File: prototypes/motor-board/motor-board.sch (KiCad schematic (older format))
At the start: 15 parts, among them J1 Conn_01x02, J2 Conn_01x02, J3 Conn_01x01, M1 Motor_DC, U1 TLV9051, U2 TB67H450FNG

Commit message: Correct sense resistor value
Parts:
- R3: value 1R2 -> 400m
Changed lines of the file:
@@
 P 4200 4125
 F 0 "R3" H 4270 4171 50  0000 L CNN
-F 1 "1R2" H 4270 4080 50  0000 L CNN
+F 1 "400m" H 4270 4080 50  0000 L CNN
 F 2 "" V 4130 4125 50  0001 C CNN
 F 3 "~" H 4200 4125 50  0001 C CNN

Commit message: Add some footprints to library symbols
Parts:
- R1, R2, R3, R4, R5, R6: footprint (none) -> mini-mapper:R_0805
- U2: footprint (none) -> mini-mapper:SOIC127P600X175-9N
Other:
- note added: "Current limiting reference voltage"
- note added: "Current sense resistor"
- note added: "Current: 0 ≤ I ≤ 250 mA\nKeep Vsense ≤ 100 mV\n\nRsense = 0.4 Ω ⇒\n 0 ≤ Vsense ≤ 0.1 V\n\n(Pmax = 25 mW)\n"
- note added: "Iout(max) = 0.1 Vref / Rsense\n\nWant Iout(max) = 250 mA\nwith VM = 4.5 V\n\nSetting Rsense = 0.4 Ω\n\nVref = 10 x 0.25 x 0.4 = 1 V\n"
- note removed: "Current sense resistor\nCurrent: 0 ≤ I ≤ 250 mA\nKeep Vsense ≤ 100 mV\nMax Rsense = 0.4 Ω ⇒\n 0 ≤ V ≤ 0.1 V\n(Pmax = 25 mW)\n"
- note removed: "Set current limiting\nreference voltage\n\nIout(max) = 0.1 Vref / Rsense\n\nWant Iout(max) = 250 mA\nwith VM = 4.5 V\n\nWith Rsense = 0.4 Ω\n\nVref = 10 x 0.25 x 0.4 = 1 V\n"
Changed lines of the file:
@@
 F 0 "U2" H 4200 3825 50  0000 C CNN
 F 1 "TB67H450FNG" H 4000 3500 50  0000 C CNN
-F 2 "" H 4100 3300 50  0001 C CNN
-F 3 "" H 4100 3300 50  0001 C CNN
+F 2 "mini-mapper:SOIC127P600X175-9N" H 4100 3300 50  0001 C CNN
+F 3 "https://www.mouser.com/pdfDocs/TB67H450FNG_datasheet_en_20190401.pdf" H 4100 3300 50  0001 C CNN
 	1    4000 3350
 	1    0    0    -1
@@
 F 0 "R3" H 4270 4171 50  0000 L CNN
 F 1 "400m" H 4270 4080 50  0000 L CNN
-F 2 "" V 4130 4125 50  0001 C CNN
+F 2 "mini-mapper:R_0805" V 4130 4125 50  0001 C CNN
 F 3 "~" H 4200 4125 50  0001 C CNN
 	1    4200 4125
@@
 Wire Wire Line
 	4000 4350 4000 4400
-Text Notes 3650 5175 0    50   ~ 0
-Current sense resistor\nCurrent: 0 ≤ I ≤ 250 mA\nKeep Vsense ≤ 100 mV\nMax Rsense = 0.4 Ω ⇒\n   0 ≤ V ≤ 0.1 V\n(Pmax = 25 mW)\n
+Text Notes 3625 4800 0    50   Italic 10
+Current sense resistor
 $Comp
 L mini-mapper:VM #PWR09
@@
 F 0 "R1" H 2820 4021 50  0000 L CNN
 F 1 "7K" H 2820 3930 50  0000 L CNN
-F 2 "" V 2680 3975 50  0001 C CNN
+F 2 "mini-mapper:R_0805" V 2680 3975 50  0001 C CNN
 F 3 "~" H 2750 3975 50  0001 C CNN
 	1    2750 3975
@@
 F 0 "R2" H 2820 4421 50  0000 L CNN
 F 1 "2K" H 2820 4330 50  0000 L CNN
-F 2 "" V 2680 4375 50  0001 C CNN
+F 2 "mini-mapper:R_0805" V 2680 4375 50  0001 C CNN
 F 3 "~" H 2750 4375 50  0001 C CNN
 	1    2750 4375
@@
 Wire Wire Line
 	3150 4650 3150 4625
-Text Notes 1375 4900 0    50   ~ 0
-Set current limiting\nreference voltage\n\nIout(max) = 0.1 Vref / Rsense\n\nWant Iout(max) = 250 mA\nwith VM = 4.5 V\n\nWith Rsense = 0.4 Ω\n\nVref = 10 x 0.25 x 0.4 = 1 V\n
+Text Notes 1125 3850 0    50   Italic 10
+Current limiting reference voltage
 Wire Wire Line
 	2875 2675 3375 2675
@@
 F 0 "R6" H 5430 4729 50  0000 R CNN
 F 1 "220K" H 5430 4820 50  0000 R CNN
-F 2 "" V 5430 4775 50  0001 C CNN
+F 2 "mini-mapper:R_0805" V 5430 4775 50  0001 C CNN
 F 3 "~" H 5500 4775 50  0001 C CNN
 	1    5500 4775
@@
 F 0 "R5" H 5330 4254 50  0000 R CNN
 F 1 "330K" H 5330 4345 50  0000 R CNN
-F 2 "" V 5330 4300 50  0001 C CNN
+F 2 "mini-mapper:R_0805" V 5330 4300 50  0001 C CNN
 F 3 "~" H 5400 4300 50  0001 C CNN
 	1    5400 4300
@@
 F 0 "R4" H 5475 4725 50  0000 R CNN
 F 1 "12K" H 5525 4825 50  0000 R CNN
-F 2 "" V 5230 4775 50  0001 C CNN
+F 2 "mini-mapper:R_0805" V 5230 4775 50  0001 C CNN
 F 3 "~" H 5300 4775 50  0001 C CNN
 	1    5300 4775
@@
 Text Label 5850 4050 0    50   ~ 0
 Vsense
+Text Notes 3625 5400 0    50   ~ 0
+Current: 0 ≤ I ≤ 250 mA\nKeep Vsense ≤ 100 mV\n\nRsense = 0.4 Ω ⇒\n   0 ≤ Vsense ≤ 0.1 V\n\n(Pmax = 25 mW)\n
+Text Notes 1125 4575 0    50   ~ 0
+Iout(max) = 0.1 Vref / Rsense\n\nWant Iout(max) = 250 mA\nwith VM = 4.5 V\n\nSetting Rsense = 0.4 Ω\n\nVref = 10 x 0.25 x 0.4 = 1 V\n
 $EndSCHEMATC

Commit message: Add some more footprints; set up link field for symbols
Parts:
- C2, C3: footprint (none) -> mini-mapper:C_0805
- U1: footprint (none) -> mini-mapper:SOT-23-5; Link (none) -> https://www.ti.com/product/TLV9052; MPN (none) -> TLV9051IDBVR
- U1: footprint (none) -> mini-mapper:SOT-23-5
- U2: Link (none) -> https://toshiba.semicon-storage.com/us/semiconductor/produc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; MPN (none) -> TB67H450FNG
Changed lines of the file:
@@
 F 2 "mini-mapper:SOIC127P600X175-9N" H 4100 3300 50  0001 C CNN
 F 3 "https://www.mouser.com/pdfDocs/TB67H450FNG_datasheet_en_20190401.pdf" H 4100 3300 50  0001 C CNN
+F 4 "TB67H450FNG" H 4000 3350 50  0001 C CNN "MPN"
+F 5 "https://toshiba.semicon-storage.com/us/semiconductor/product/motor-driver-ics/brushed-dc-motor-driver-ics/detail.TB67H450FNG.html" H 4000 3350 50  0001 C CNN "Link"
 	1    4000 3350
 	1    0    0    -1
@@
 F 0 "C3" H 3490 2921 50  0000 L CNN
 F 1 "0.1U" H 3490 2830 50  0000 L CNN
-F 2 "" H 3413 2725 50  0001 C CNN
+F 2 "mini-mapper:C_0805" H 3413 2725 50  0001 C CNN
 F 3 "~" H 3375 2875 50  0001 C CNN
 	1    3375 2875
@@
 F 0 "C2" H 3265 4521 50  0000 L CNN
 F 1 "0.1U" H 3265 4430 50  0000 L CNN
-F 2 "" H 3188 4325 50  0001 C CNN
+F 2 "mini-mapper:C_0805" H 3188 4325 50  0001 C CNN
 F 3 "~" H 3150 4475 50  0001 C CNN
 	1    3150 4475
@@
 F 0 "U1" H 5025 4275 50  0000 C CNN
 F 1 "TLV9051" H 5025 3800 50  0000 C CNN
-F 2 "" H 5025 4050 50  0001 C CNN
-F 3 "www.st.com/resource/en/datasheet/tsv911.pdf" H 5025 4050 50  0001 C CNN
+F 2 "mini-mapper:SOT-23-5" H 5025 4050 50  0001 C CNN
+F 3 "https://www.ti.com/lit/ds/symlink/tlv9052.pdf" H 5025 4050 50  0001 C CNN
+F 4 "TLV9051IDBVR" H 5025 4050 50  0001 C CNN "MPN"
+F 5 "https://www.ti.com/product/TLV9052" H 5025 4050 50  0001 C CNN "Link"
 	1    5025 4050
 	1    0    0    -1
@@
 F 0 "U1" H 3803 6246 50  0000 L CNN
 F 1 "TLV9051" H 3803 6155 50  0000 L CNN
-F 2 "" H 3775 6200 50  0001 C CNN
-F 3 "www.st.com/resource/en/datasheet/tsv911.pdf" H 3775 6200 50  0001 C CNN
+F 2 "mini-mapper:SOT-23-5" H 3775 6200 50  0001 C CNN
+F 3 "https://www.ti.com/lit/ds/symlink/tlv9052.pdf" H 3775 6200 50  0001 C CNN
 	2    3775 6200
 	1    0    0    -1

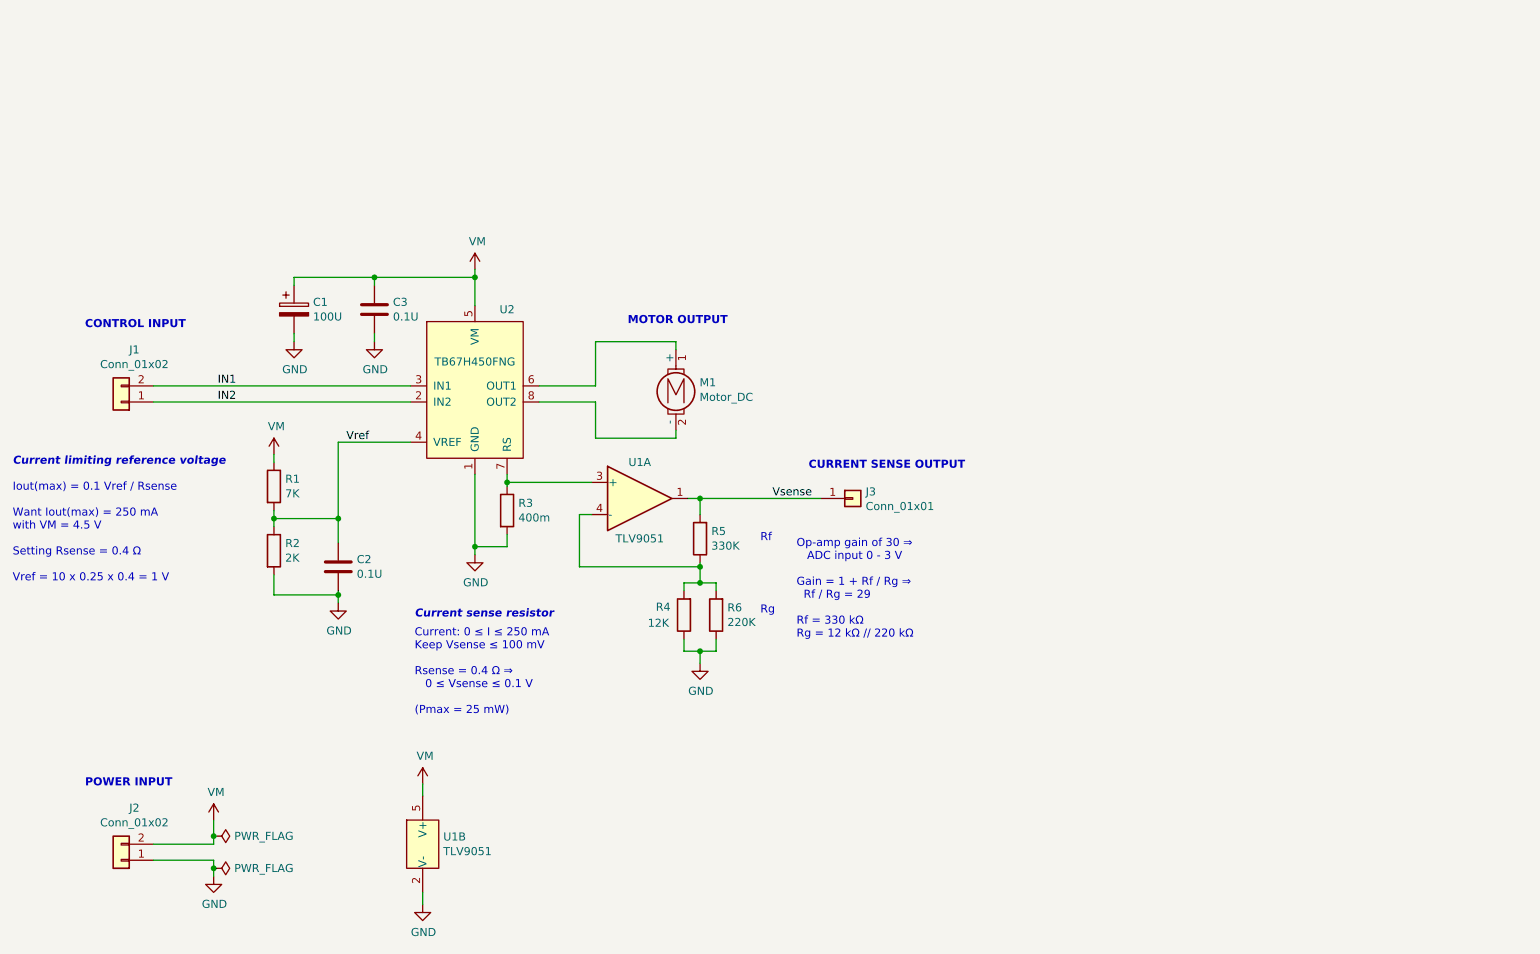
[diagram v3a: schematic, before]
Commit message: Small improvements to motor prototype schematic
 - Move motor off board
 - Set up to route current sensing connection as differential pair
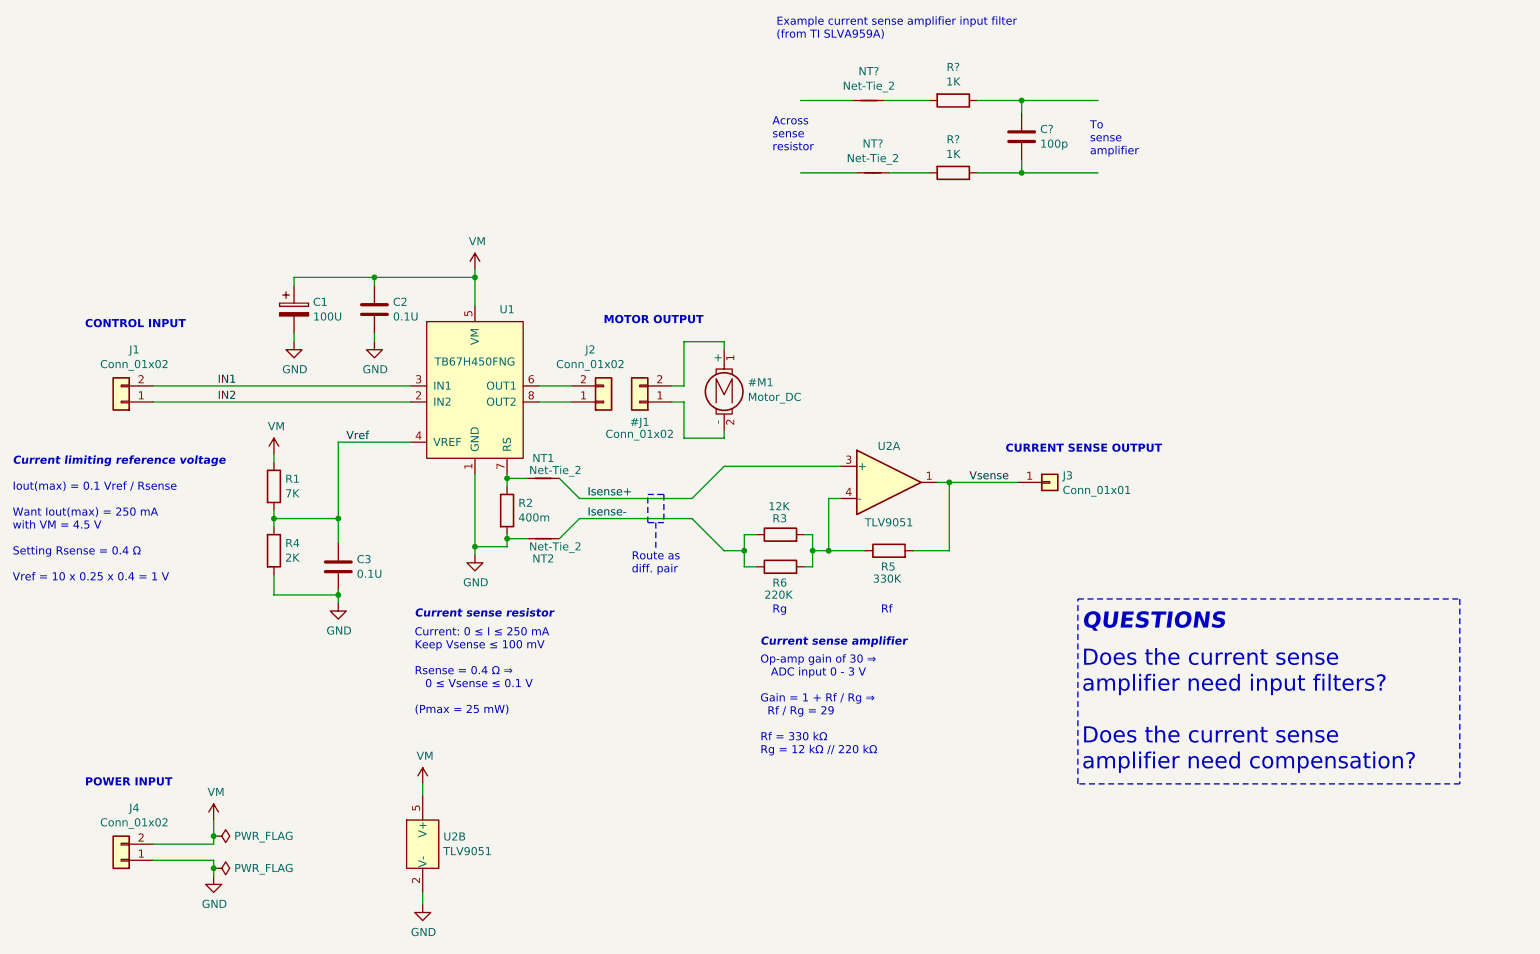
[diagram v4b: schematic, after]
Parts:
- removed M1: Motor_DC, symbol mini-mapper:Motor_DC
- added C?: 100p, mini-mapper:C_0805, symbol mini-mapper:C
- added J2: Conn_01x02, symbol mini-mapper:Conn_01x02
- added NT1, NT2, NT? (x2): Net-Tie_2, symbol Device:Net-Tie_2
- added R? (x2): 1K, mini-mapper:R_0805, symbol mini-mapper:R
- renumbered C3 to C2, C2 to C3, J2 to J4, R3 to R2, R4 to R3, R2 to R4, U2 to U1, U1 to U2
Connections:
- net labels added: Conn_01x02, Isense+, Isense-, Motor_DC
- wire segments 61 -> 82
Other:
- note added: "Across\nsense\nresistor"
- note added: "Current sense amplifier"
- note added: "Does the current sense\namplifier need input filters?\n\nDoes the current sense\namplifier need compensation?"
- note added: "Example current sense amplifier input filter\n(from TI SLVA959A)"
- note added: "QUESTIONS"
- note added: "Route as\ndiff. pair"
- note added: "To\nsense\namplifier"
- moved on the sheet: J3, R3, R5, R6, U2A
